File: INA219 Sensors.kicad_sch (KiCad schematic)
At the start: 11 parts, among them J1 BAT/PWR IN, U2 INA219AxD, U3 INA219AxD

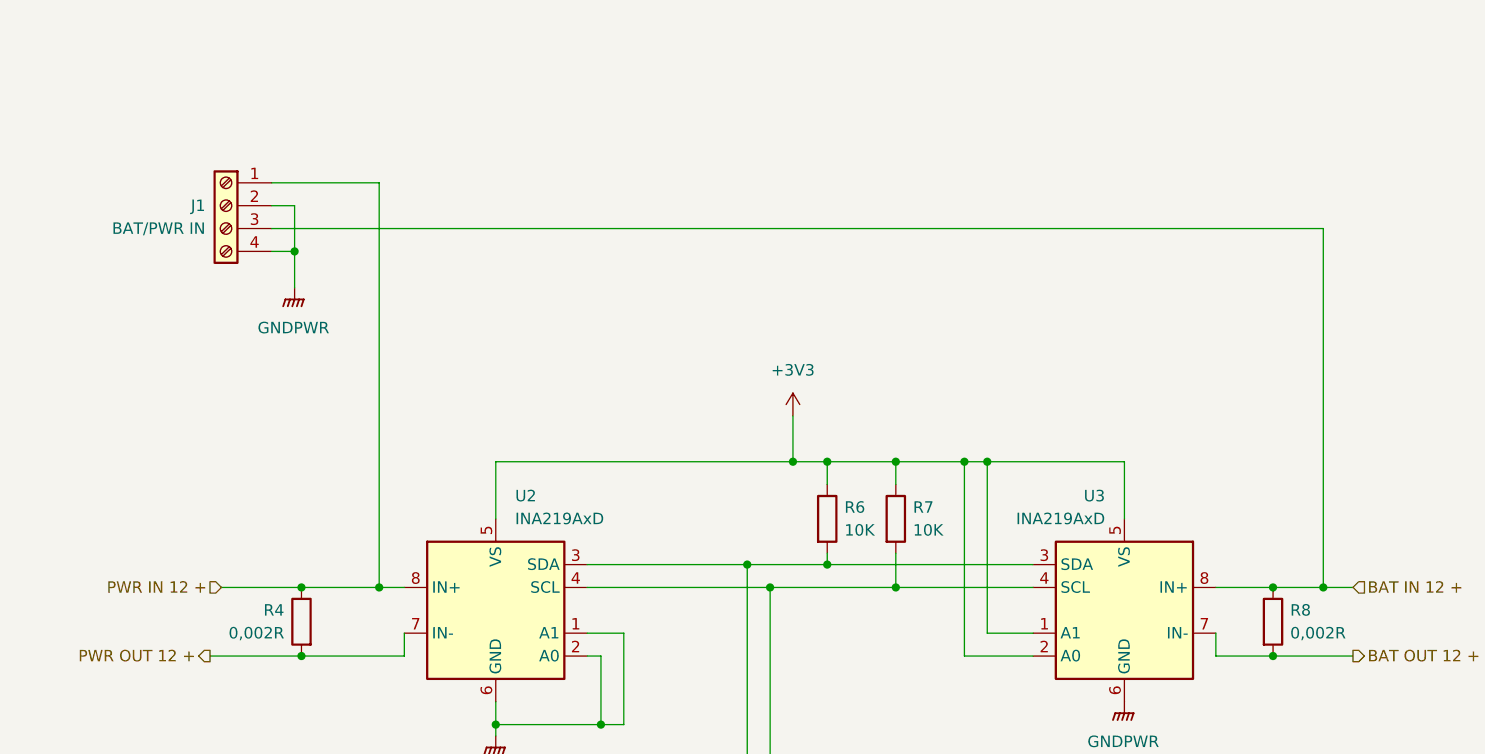
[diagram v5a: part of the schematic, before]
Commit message: Add poert switch
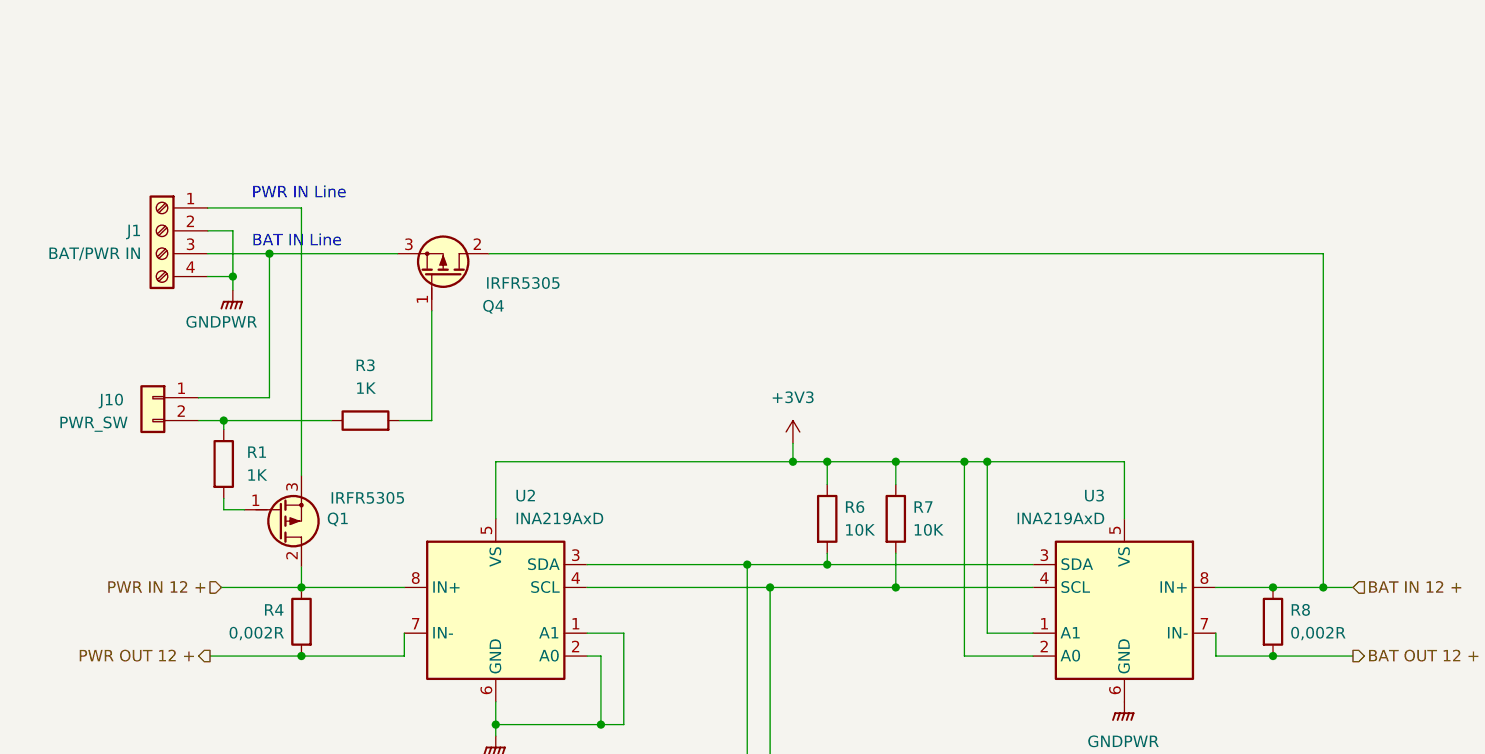
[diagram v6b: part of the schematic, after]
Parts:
- added J10: PWR_SW, Connector_JST:JST_PH_B2B-PH-K_1x02_P2.00mm_Vertical, symbol Connector_Generic:Conn_01x02
- added Q1, Q4: IRFR5305, PCM_Package_TO_SOT_SMD_AKL:TO-252-2, symbol PCM_Transistor_MOSFET_AKL:IRFR5305
- added R1, R3: 1K, Resistor_SMD:R_0805_2012Metric_Pad1.20x1.40mm_HandSolder, symbol Device:R
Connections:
- net BAT IN 12 +: now also Q4.2 (D); no longer J1.3 (Pin_3)
- net PWR IN 12 +: now also Q1.2 (D); no longer J1.1 (Pin_1)
- new net: J1.3 (Pin_3), J10.1 (Pin_1), Q4.3 (S)
- new net: J10.2 (Pin_2), R1.1, R3.1
- new net: Q1.1 (G), R1.2
- new net: J1.1 (Pin_1), Q1.3 (S)
- new net: Q4.1 (G), R3.2
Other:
- note added: "BAT IN Line"
- note added: "PWR IN Line"
- moved on the sheet: J1
